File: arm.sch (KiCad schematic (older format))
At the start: 91 parts, among them J1 MICROSD_SOCKET_SPI, M1 MOTOR, P1 MicroUSB, P2 HC-05/06, P3 I²C_Port, P4 SPI_Port, Q1 MOSFET_N, Q2 IRLML2246TRPBF, Q3 IRLML2246TRPBF, Q5 IRLML2246TRPBF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

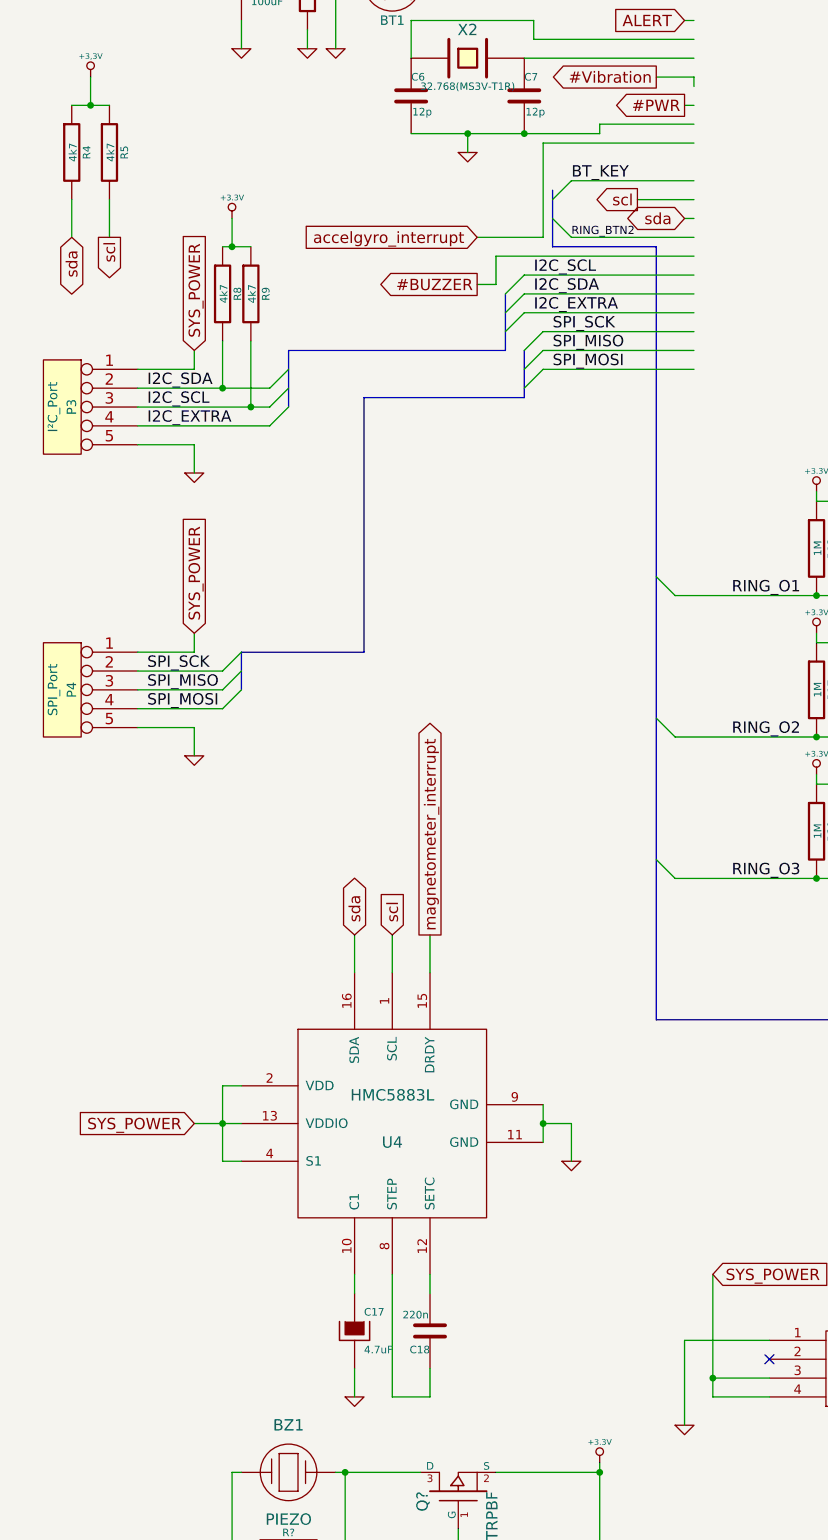
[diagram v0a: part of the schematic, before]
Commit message: SPI_NSS, extra components for soldering
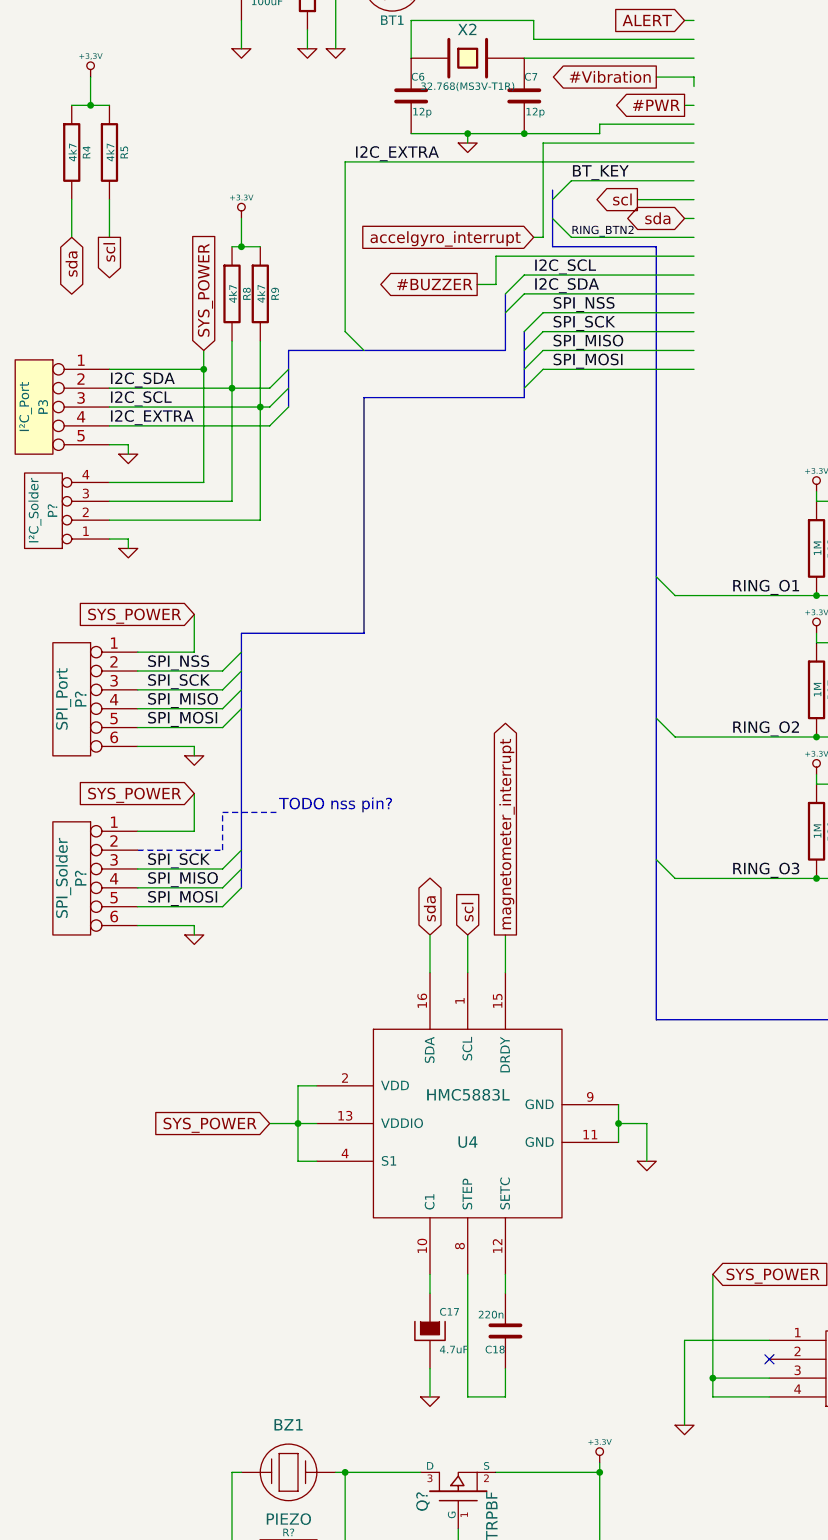
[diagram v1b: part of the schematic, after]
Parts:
- removed P4: SPI_Port, symbol CONN_5
- added P?: SPI_Port, symbol CONN_6
- added P?: SPI_Solder, symbol CONN_6
- added P?: I²C_Solder, symbol CONN_4
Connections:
- net labels added: SPI_NSS
- wire segments 354 -> 369
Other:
- note added: "TODO nss pin?"
- moved on the sheet: C17, C18, P3, R8, R9, U4

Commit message: i2c pullups set to sys_power, modified firmware switch
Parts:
- removed R1: 10k, ~, symbol R
- removed SW1: BTN Function (FW/RST), ~, symbol SPST
- added SW?: SWITCH_INV, ~, symbol SWITCH_INV
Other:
- moved on the sheet: Q1, R4, R5
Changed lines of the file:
@@
-$EndComp
-$Comp
-L R R1
-U 1 1 52C0BE22
-P 15500 10000
-F 0 "R1" V 15580 10000 40  0000 C CNN
-F 1 "10k" V 15507 10001 40  0000 C CNN
-F 2 "~" V 15430 10000 30  0000 C CNN
-F 3 "~" H 15500 10000 30  0000 C CNN
-	1    15500 10000
-	-1   0    0    1
 $EndComp
 $Comp
 L GND #PWR13
 U 1 1 52C0BEB6
-P 15500 10350
-F 0 "#PWR13" H 15500 10350 30  0001 C CNN
-F 1 "GND" H 15500 10280 30  0001 C CNN
-F 2 "" H 15500 10350 60  0000 C CNN
-F 3 "" H 15500 10350 60  0000 C CNN
-	1    15500 10350
+P 15700 10300
+F 0 "#PWR13" H 15700 10300 30  0001 C CNN
+F 1 "GND" H 15700 10230 30  0001 C CNN
+F 2 "" H 15700 10300 60  0000 C CNN
+F 3 "" H 15700 10300 60  0000 C CNN
+	1    15700 10300
 	1    0    0    -1
 $EndComp
@@
 L R R4
 U 1 1 52C18407
-P 800 3100
-F 0 "R4" V 880 3100 40  0000 C CNN
-F 1 "4k7" V 807 3101 40  0000 C CNN
-F 2 "~" V 730 3100 30  0000 C CNN
-F 3 "~" H 800 3100 30  0000 C CNN
-	1    800  3100
+P 800 3350
+F 0 "R4" V 880 3350 40  0000 C CNN
+F 1 "4k7" V 807 3351 40  0000 C CNN
+F 2 "~" V 730 3350 30  0000 C CNN
+F 3 "~" H 800 3350 30  0000 C CNN
+	1    800  3350
 	1    0    0    -1
 $EndComp
@@
 L R R5
 U 1 1 52C18416
-P 1000 3100
-F 0 "R5" V 1080 3100 40  0000 C CNN
-F 1 "4k7" V 1007 3101 40  0000 C CNN
-F 2 "~" V 930 3100 30  0000 C CNN
-F 3 "~" H 1000 3100 30  0000 C CNN
-	1    1000 3100
-	1    0    0    -1
-$EndComp
-$Comp
-L +3,3V #PWR10
-U 1 1 52C184F0
-P 900 2700
-F 0 "#PWR10" H 900 2660 30  0001 C CNN
-F 1 "+3,3V" H 900 2810 30  0000 C CNN
-F 2 "" H 900 2700 60  0000 C CNN
-F 3 "" H 900 2700 60  0000 C CNN
-	1    900  2700
+P 1000 3350
+F 0 "R5" V 1080 3350 40  0000 C CNN
+F 1 "4k7" V 1007 3351 40  0000 C CNN
+F 2 "~" V 930 3350 30  0000 C CNN
+F 3 "~" H 1000 3350 30  0000 C CNN
+	1    1000 3350
 	1    0    0    -1
 $EndComp
@@
 Text GLabel 1450 5550 0    60   Input ~ 0
 SYS_POWER
-Text GLabel 1500 4150 1    60   Input ~ 0
+Text GLabel 1500 2950 1    60   Input ~ 0
 SYS_POWER
 $Comp
@@
 F 3 "~" H 1800 3850 30  0000 C CNN
 	1    1800 3850
-	1    0    0    -1
-$EndComp
-$Comp
-L +3.3V #PWR14
-U 1 1 52FBA1D9
-P 1700 3450
-F 0 "#PWR14" H 1700 3410 30  0001 C CNN
-F 1 "+3.3V" H 1700 3560 30  0000 C CNN
-F 2 "" H 1700 3450 60  0000 C CNN
-F 3 "" H 1700 3450 60  0000 C CNN
-	1    1700 3450
 	1    0    0    -1
 $EndComp
@@
 Entry Wire Line
 	1850 4550 1950 4450
-$Comp
-L SPST SW1
-U 1 1 53080117
-P 15500 9150
-F 0 "SW1" H 15500 9250 70  0000 C CNN
-F 1 "BTN Function (FW/RST)" H 15500 9050 70  0000 C CNN
-F 2 "~" H 15500 9150 60  0000 C CNN
-F 3 "~" H 15500 9150 60  0000 C CNN
-	1    15500 9150
-	0    -1   -1   0
-$EndComp
 Entry Wire Line
 	7600 5050 7700 5150
@@
 Text Label 7150 2950 0    60   ~ 0
 SD_CD
-Text GLabel 15100 9100 1    60   Output ~ 0
+Text GLabel 14300 9050 1    60   Output ~ 0
 #BT_PWR
 Entry Wire Line
@@
 	1    0    0    -1
 $EndComp
-Text GLabel 800  3550 3    60   BiDi ~ 0
+Text GLabel 800  3800 3    60   BiDi ~ 0
 sda
-Text GLabel 1000 3550 3    60   Output ~ 0
+Text GLabel 1000 3800 3    60   Output ~ 0
 scl
 Text Label 3450 3250 0    60   ~ 0
@@
 L MOSFET_N Q1
 U 1 1 53093544
-P 15200 9700
-F 0 "Q1" H 15210 9870 60  0000 R CNN
-F 1 "MOSFET_N" H 15210 9550 60  0000 R CNN
-F 2 "~" H 15200 9700 60  0000 C CNN
-F 3 "~" H 15200 9700 60  0000 C CNN
-	1    15200 9700
+P 14400 9650
+F 0 "Q1" H 14410 9820 60  0000 R CNN
+F 1 "MOSFET_N" H 14410 9500 60  0000 R CNN
+F 2 "~" H 14400 9650 60  0000 C CNN
+F 3 "~" H 14400 9650 60  0000 C CNN
+	1    14400 9650
 	-1   0    0    -1
 $EndComp
@@
 L GND #PWR9
 U 1 1 5309384B
-P 15100 10350
-F 0 "#PWR9" H 15100 10350 30  0001 C CNN
-F 1 "GND" H 15100 10280 30  0001 C CNN
-F 2 "" H 15100 10350 60  0000 C CNN
-F 3 "" H 15100 10350 60  0000 C CNN
-	1    15100 10350
+P 14300 10300
+F 0 "#PWR9" H 14300 10300 30  0001 C CNN
+F 1 "GND" H 14300 10230 30  0001 C CNN
+F 2 "" H 14300 10300 60  0000 C CNN
+F 3 "" H 14300 10300 60  0000 C CNN
+	1    14300 10300
 	1    0    0    -1
 $EndComp
@@
 	9400 3800 10900 3800
 Wire Wire Line
-	15100 9900 15100 10350
-Wire Wire Line
-	15100 9100 15100 9500
+	14300 9850 14300 10300
+Wire Wire Line
+	14300 9050 14300 9450
 Wire Wire Line
 	8100 4400 8100 4300
@@
 	2200 2200 2200 2550
 Wire Wire Line
-	1000 3350 1000 3550
-Wire Wire Line
-	800  3350 800  3550
-Connection ~ 900  2850
-Wire Wire Line
-	900  2850 900  2700
-Wire Wire Line
-	800  2850 1000 2850
+	1000 3600 1000 3800
+Wire Wire Line
+	800  3600 800  3800
+Connection ~ 900  3100
+Wire Wire Line
+	900  3100 900  2950
+Wire Wire Line
+	800  3100 1000 3100
 Wire Wire Line
 	1700 3600 1700 3450
@@
 	1450 5750 1450 5550
 Wire Wire Line
-	1500 4150 1500 4850
+	1500 2950 1500 4850
 Wire Wire Line
 	1650 4100 1650 4950
@@
 Connection ~ 3200 3000
 Wire Wire Line
-	15400 9700 15800 9700
-Wire Wire Line
-	15500 9650 15500 9750
-Wire Wire Line
-	15500 10250 15500 10350
-Connection ~ 15500 9700
+	15700 9750 15700 10300
 $Comp
 L +3.3V #PWR?
 U 1 1 5395FCE4
-P 15500 8600
-F 0 "#PWR?" H 15500 8560 30  0001 C CNN
-F 1 "+3.3V" H 15500 8710 30  0000 C CNN
-F 2 "" H 15500 8600 60  0000 C CNN
-F 3 "" H 15500 8600 60  0000 C CNN
-	1    15500 8600
-	1    0    0    -1
-$EndComp
-Wire Wire Line
-	15500 8600 15500 8650
-Text GLabel 15800 9100 1    60   Output ~ 0
+P 15700 9000
+F 0 "#PWR?" H 15700 8960 30  0001 C CNN
+F 1 "+3.3V" H 15700 9110 30  0000 C CNN
+F 2 "" H 15700 9000 60  0000 C CNN
+F 3 "" H 15700 9000 60  0000 C CNN
+	1    15700 9000
+	1    0    0    -1
+$EndComp
+Wire Wire Line
+	15700 9000 15700 9550
+Text GLabel 14650 9050 1    60   Output ~ 0
 FW/RST
 Wire Wire Line
-	15800 9700 15800 9100
+	14650 9650 14650 9050
 Wire Wire Line
 	2250 1650 4100 1650
@@
 Wire Notes Line
 	1600 6600 1900 6600
+Text GLabel 900  2950 1    60   Input ~ 0
+SYS_POWER
+Wire Wire Line
+	1700 3450 1500 3450
+Connection ~ 1500 3450
+$Comp
+L SWITCH_INV SW?
+U 1 1 539F1B21
+P 15200 9650
+F 0 "SW?" H 15000 9800 50  0000 C CNN
+F 1 "SWITCH_INV" H 15050 9500 50  0000 C CNN
+F 2 "~" H 15200 9650 60  0000 C CNN
+F 3 "~" H 15200 9650 60  0000 C CNN
+	1    15200 9650
+	1    0    0    -1
+$EndComp
+Wire Wire Line
+	14600 9650 14700 9650
+Connection ~ 14650 9650
 $EndSCHEMATC
